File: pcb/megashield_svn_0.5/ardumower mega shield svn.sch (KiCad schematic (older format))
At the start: 88 parts, among them K1 Tilt sens, K2 Button, K3 RELAY_2RT, P1 Sonar C, P10 GPS, P11 Bumper, P12 PerimeterRight, P13 RC Remote, P14 User switch, P15 Dual2-M1Out, P16 Dual2-pwr, P17 Dual1-pwr, P18 Mow Motor, P19 DS1307, P2 Sonar R, P20 Wlan, P21 DropRight, P3 Sonar L, P4 Rain, P5 IMU Kompas, P6 Lawn sens, P7 Status LEDs, P8 ODO Right, P9 ODO Left, U1 DC-DC, U2 HC05_Bluetooth, U3 INA169 Adafruit

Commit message: Pufferkondensator 3,3V + 5,5V , Spannungsleiste 3,3V +5V +GND, Pins unbenutzte Kontakte hinzugefügt Regensensor hat jetzt auch 5V + kleine Änderungen
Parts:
- removed P4: Rain, Pin_Headers:Pin_Header_Straight_1x02, symbol CONN_2
- added C? (x2): ??, Capacitors_ThroughHole:Capacitor3MMDiscRM2.5, symbol CP1
- added JP?: 5V, Connect:PINHEAD1-2, symbol JUMPER
- added JP?: 3,3V, Connect:PINHEAD1-2, symbol JUMPER
- added P4: Rain, Pin_Headers:Pin_Header_Straight_1x03, symbol CONN_3
- added P? (x5): CONN_01X01, symbol CONN_01X01
- added P?: Stromleiste 5V, symbol CONN_01X08
- added P?: Stromleiste GND, symbol CONN_01X08
- added P?: Stromleiste 3,3V, symbol CONN_01X08
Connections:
- net +3.3V: now also C?.1, JP?.1, P?.1 (P1), P?.2 (P2), P?.3 (P3), P?.4 (P4), P?.5 (P5), P?.6 (P6), P?.7 (P7), P?.8 (P8)
- net +5V: now also C?.1, JP?.1, P4.1 (P1), P?.1 (P1), P?.2 (P2), P?.3 (P3), P?.4 (P4), P?.5 (P5), P?.6 (P6), P?.7 (P7), P?.8 (P8); no longer U2.6 (VCC)
- net GND: now also C?.2, C?.2, P4.3 (P3), P?.1 (P1), P?.2 (P2), P?.3 (P3), P?.4 (P4), P?.5 (P5), P?.6 (P6), P?.7 (P7), P?.8 (P8)
- net pinRain: now also P4.2 (PM)
- net at SHIELD1.0 (RX0): now also P?.1 (P1)
- net at SHIELD1.1 (TX0): now also P?.1 (P1)
- net at SHIELD1.4: now also P?.1 (P1)
- net at SHIELD1.8: now also P?.1 (P1)
- net at SHIELD1.9: now also P?.1 (P1)
- new net: JP?.2, JP?.2, U2.6 (VCC)
- no-connect marks 41 -> 36
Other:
- note added: "Abgriff 5V, 3V, GND"
- note added: "Pufferkondensator 3,3v und 5V\ndamit könten eigentlich die\neinzelnen Kondensatoren entfallen.\nz.B bei den INA"
- note removed: "VCC muss das nicht auch 3.3V sein\n?????????????????????????????"
- moved on the sheet: R1, R2, R5, R?

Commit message: Änderungen am Schaltplan, Footprint und PCB Achtung Relais fehlerhaft ! Anordung der Bauteile muss noch Feintunig erfolgen
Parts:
- removed C? (x2): ??, Capacitors_ThroughHole:Capacitor3MMDiscRM2.5, symbol CP1
- P22, P23, P24, P25, P26, P27, P28, P29: renamed from P?; footprint (none) -> Pin_Headers:Pin_Header_Straight_1x01
- P32, P33, P34: renamed from P?; footprint (none) -> Pin_Headers:Pin_Header_Straight_1x08
- P4: footprint Pin_Headers:Pin_Header_Straight_1x03 -> Pin_Headers:Pin_Header_Straight_1x02
- P7: footprint (none) -> Pin_Headers:Pin_Header_Straight_1x04
- Q1: renamed from Q?; footprint TO92-EBC -> Discret:TO92-EBC
- R18: renamed from R?; footprint (none) -> Resistors_ThroughHole:Resistor_Horizontal_RM15mm
- RR2: footprint Pin_Headers:Pin_Header_Straight_1x04 -> Pin_Headers:Pin_Header_Straight_1x09
- gave numbers to parts that had none: 26
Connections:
- net GND: now also K1.2 (PM), P1.2 (P2), P2.2 (P2), P3.2 (P2), P30.2 (PM), P4.2 (PM), P5.2 (P2), P8.2 (P2), P9.2 (P2); no longer K1.3 (P3), P1.4 (P4), P2.4 (P4), P3.4 (P4), P30.3 (P3), P4.3 (P3), P5.4 (P4), P8.4 (P4), P9.4 (P4)
- net SCL1: now also P5.4 (P4); no longer P5.3 (P3)
- net SDA1: now also P5.3 (P3); no longer P5.2 (P2)
- net pinBatteryVoltage: now also RP1.11 (R6); no longer RP1.3 (P3)
- net pinChargeCurrent: now also RP2.9 (R8); no longer RP2.1 (P1)
- net pinChargeVoltage: now also RP2.10 (R7); no longer RP2.2 (P2)
- net pinChargingBilanz: now also RP2.11 (R6); no longer RP2.3 (P3)
- net pinMotorLeftSense: now also RP1.10 (R7); no longer RP1.2 (P2)
- net pinMotorMowSense: now also RP1.12 (R5); no longer RP1.4 (P4)
- net pinMotorRightSense: now also RP1.9 (R8); no longer RP1.1 (P1)
- net pinOdometryLeft: now also P9.3 (P3), RP2.13 (R4); no longer P9.2 (P2), RP2.5 (P5)
- net pinOdometryLeft2: now also P9.4 (P4), RP2.14 (R3); no longer P9.3 (P3), RP2.6 (P6)
- net pinOdometryRight: now also P8.3 (P3), RP2.15 (R2); no longer P8.2 (P2), RP2.8 (P8)
- net pinOdometryRight2: now also P8.4 (P4), RP2.16 (R1); no longer P8.3 (P3), RP2.7 (P7)
- net pinPerimeterLeft: now also RP1.14 (R3); no longer RP1.6 (P6)
- net pinPerimeterRight: now also P30.3 (P3), RP1.13 (R4); no longer P30.2 (PM), RP1.5 (P5)
- net pinRain: now also P4.3 (P3); no longer P4.2 (PM)
- net pinSonarCenterEcho: now also P1.4 (P4); no longer P1.3 (P3)
- net pinSonarCenterTrigger: now also P1.3 (P3); no longer P1.2 (P2)
- net pinSonarLeftEcho: now also P3.4 (P4); no longer P3.3 (P3)
- net pinSonarLeftTrigger: now also P3.3 (P3); no longer P3.2 (P2)
- net pinSonarRightEcho: now also P2.4 (P4); no longer P2.3 (P3)
- net pinSonarRightTrigger: now also P2.3 (P3); no longer P2.2 (P2)
- net pinTilt: now also K1.3 (P3); no longer K1.2 (PM)
- net at RR1.2, SHIELD1.AD0: now also RP1.8 (P8); no longer RP1.16 (R1)
- net at RR1.3, SHIELD1.AD1: now also RP1.7 (P7); no longer RP1.15 (R2)
- net at RR2.4, SHIELD1.AD10: now also RP2.6 (P6); no longer RP2.14 (R3)
- net at RR2.5, SHIELD1.AD11: now also RP2.5 (P5); no longer RP2.13 (R4)
- net at RR2.6, SHIELD1.AD12: now also RP2.4 (P4); no longer RP2.12 (R5)
- net at RR2.7, SHIELD1.AD13: now also RP2.3 (P3); no longer RP2.11 (R6)
- net at RR2.8, SHIELD1.AD14: now also RP2.2 (P2); no longer RP2.10 (R7)
- net at RR2.9, SHIELD1.AD15: now also RP2.1 (P1); no longer RP2.9 (R8)
- net at RR1.4, SHIELD1.AD2: now also RP1.6 (P6); no longer RP1.14 (R3)
- net at RR1.5, SHIELD1.AD3: now also RP1.5 (P5); no longer RP1.13 (R4)
- net at RR1.6, SHIELD1.AD4: now also RP1.4 (P4); no longer RP1.12 (R5)
- net at RR1.7, SHIELD1.AD5: now also RP1.3 (P3); no longer RP1.11 (R6)
- net at RR1.8, SHIELD1.AD6: now also RP1.2 (P2); no longer RP1.10 (R7)
- net at RR1.9, SHIELD1.AD7: now also RP1.1 (P1); no longer RP1.9 (R8)
- net at RR2.2, SHIELD1.AD8: now also RP2.8 (P8); no longer RP2.16 (R1)
- net at RR2.3, SHIELD1.AD9: now also RP2.7 (P7); no longer RP2.15 (R2)
- net at P22.1 (P1): now also RP1.15 (R2); no longer RP1.7 (P7)
- net at P23.1 (P1): now also RP1.16 (R1); no longer RP1.8 (P8)
- net at P24.1 (P1): now also RP2.12 (R5); no longer RP2.4 (P4)
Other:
- note removed: "Pufferkondensator 3,3v und 5V\ndamit könten eigentlich die\neinzelnen Kondensatoren entfallen.\nz.B bei den INA"

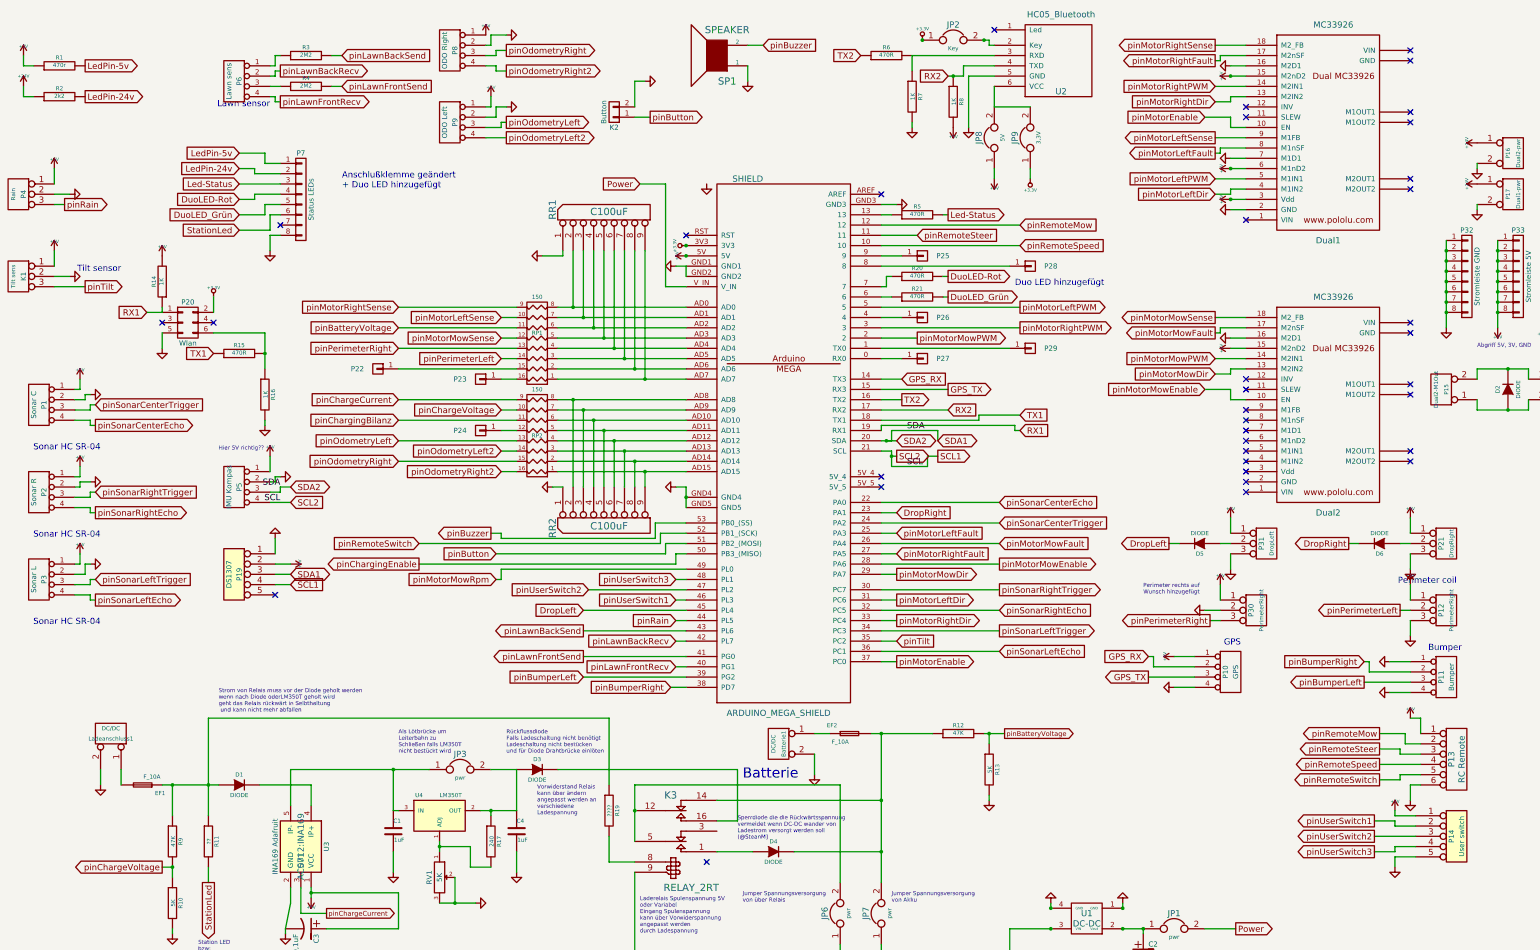
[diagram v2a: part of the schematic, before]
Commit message: Angefangen Platinenlayout zu erstellen Fehler vorhanden die Netzlinien der 2 INA169 enden an der Schraubenbefestigung und nicht an den Klemmen Der Footprint von P7 Status LED ist nur 4 Fach muss 8 fach sein Der Footprint von den Jumpern J2, J8, J9 ist falsch - zu groß der muss kleiner sein wie die anderen Jumper Kann selber die Footprints nicht zuordnen. Ich bekomme immer eine Fehlermeldung mit einen "Bibliothek Pfad" der wahrscheinlich auf ein Ordner von Stefan seine Festplatte verweist.
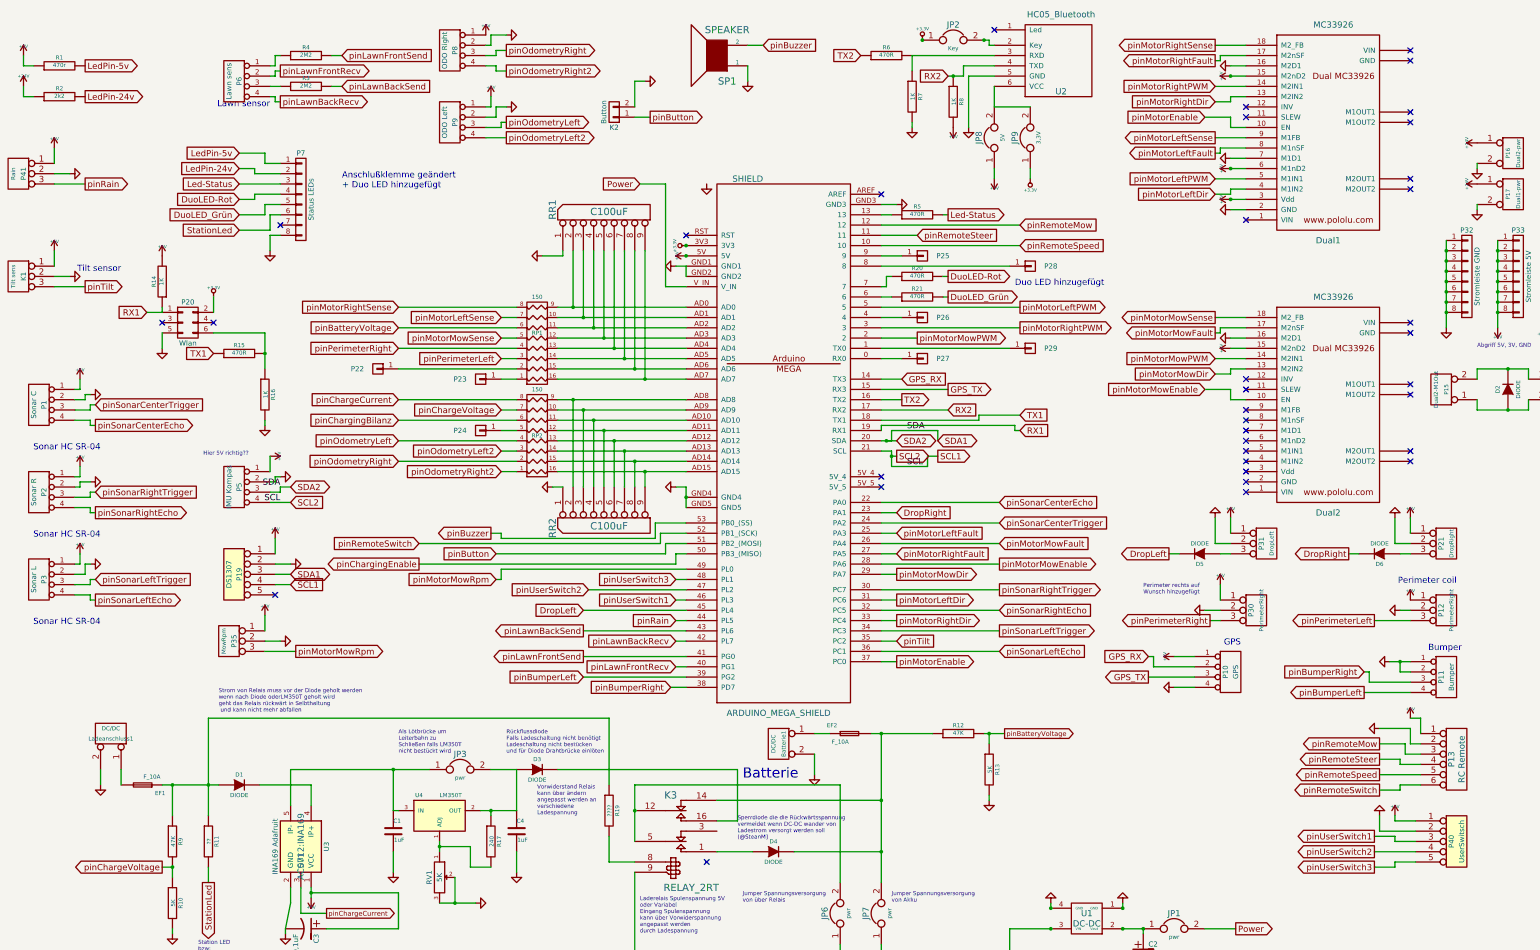
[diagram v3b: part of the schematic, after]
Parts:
- removed P14: User switch, Pin_Headers:Pin_Header_Straight_1x06, symbol CONN_5
- removed P4: Rain, Pin_Headers:Pin_Header_Straight_1x02, symbol CONN_3
- added P35: MowRpm, Pin_Headers:Pin_Header_Straight_1x03, symbol CONN_3
- added P40: UserSwitsch, Pin_Headers:Pin_Header_Straight_1x05, symbol CONN_5
- added P41: Rain, Pin_Headers:Pin_Header_Straight_1x03, symbol CONN_3
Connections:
- net +5V: now also P19.1, P35.1 (P1), P40.1, P41.1 (P1); no longer P19.2
- net GND: now also P11.2 (P2), P12.2 (PM), P13.2, P19.2, P21.2 (PM), P31.2 (PM), P35.2 (PM), P40.2, P41.2 (PM); no longer P11.4 (P4), P12.3 (P3), P13.6, P19.1, P21.3 (P3), P31.3 (P3)
- net pinBatteryVoltage: now also RP1.6 (P6); no longer RP1.11 (R6)
- net pinBumperLeft: now also P11.4 (P4); no longer P11.3 (P3)
- net pinBumperRight: now also P11.3 (P3); no longer P11.2 (P2)
- net pinChargeCurrent: now also RP2.8 (P8); no longer RP2.9 (R8)
- net pinChargeVoltage: now also RP2.7 (P7); no longer RP2.10 (R7)
- net pinChargingBilanz: now also RP2.6 (P6); no longer RP2.11 (R6)
- net pinLawnBackRecv: now also P6.4 (P4); no longer P6.2 (P2)
- net pinLawnFrontRecv: now also P6.2 (P2); no longer P6.4 (P4)
- net pinMotorLeftSense: now also RP1.7 (P7); no longer RP1.10 (R7)
- net pinMotorMowRpm: now also P35.3 (P3)
- net pinMotorMowSense: now also RP1.5 (P5); no longer RP1.12 (R5)
- net pinMotorRightSense: now also RP1.8 (P8); no longer RP1.9 (R8)
- net pinOdometryLeft: now also RP2.4 (P4); no longer RP2.13 (R4)
- net pinOdometryLeft2: now also RP2.3 (P3); no longer RP2.14 (R3)
- net pinOdometryRight: now also RP2.2 (P2); no longer RP2.15 (R2)
- net pinOdometryRight2: now also RP2.1 (P1); no longer RP2.16 (R1)
- net pinPerimeterLeft: now also P12.3 (P3), RP1.3 (P3); no longer P12.2 (PM), RP1.14 (R3)
- net pinPerimeterRight: now also RP1.4 (P4); no longer RP1.13 (R4)
- net pinRain: now also P41.3 (P3)
- net pinRemoteMow: now also P13.3; no longer P13.2
- net pinRemoteSpeed: now also P13.5; no longer P13.4
- net pinRemoteSteer: now also P13.4; no longer P13.3
- net pinRemoteSwitch: now also P13.6; no longer P13.5
- net pinUserSwitch1: now also P40.3
- net pinUserSwitch2: now also P40.4
- net pinUserSwitch3: now also P40.5
- net at RR1.2, SHIELD1.AD0: now also RP1.9 (R8); no longer RP1.8 (P8)
- net at RR1.3, SHIELD1.AD1: now also RP1.10 (R7); no longer RP1.7 (P7)
- net at RR2.4, SHIELD1.AD10: now also RP2.11 (R6); no longer RP2.6 (P6)
- net at RR2.5, SHIELD1.AD11: now also RP2.12 (R5); no longer RP2.5 (P5)
- net at RR2.6, SHIELD1.AD12: now also RP2.13 (R4); no longer RP2.4 (P4)
- net at RR2.7, SHIELD1.AD13: now also RP2.14 (R3); no longer RP2.3 (P3)
- net at RR2.8, SHIELD1.AD14: now also RP2.15 (R2); no longer RP2.2 (P2)
- net at RR2.9, SHIELD1.AD15: now also RP2.16 (R1); no longer RP2.1 (P1)
- net at RR1.4, SHIELD1.AD2: now also RP1.11 (R6); no longer RP1.6 (P6)
- net at RR1.5, SHIELD1.AD3: now also RP1.12 (R5); no longer RP1.5 (P5)
- net at RR1.6, SHIELD1.AD4: now also RP1.13 (R4); no longer RP1.4 (P4)
- net at RR1.7, SHIELD1.AD5: now also RP1.14 (R3); no longer RP1.3 (P3)
- net at RR1.8, SHIELD1.AD6: now also RP1.15 (R2); no longer RP1.2 (P2)
- net at RR1.9, SHIELD1.AD7: now also RP1.16 (R1); no longer RP1.1 (P1)
- net at RR2.2, SHIELD1.AD8: now also RP2.9 (R8); no longer RP2.8 (P8)
- net at RR2.3, SHIELD1.AD9: now also RP2.10 (R7); no longer RP2.7 (P7)
- net at P6.1 (P1): now also R4.1; no longer R3.1
- net at P6.3 (P3): now also R3.1; no longer R4.1
- net at P22.1 (P1): now also RP1.2 (P2); no longer RP1.15 (R2)
- net at P23.1 (P1): now also RP1.1 (P1); no longer RP1.16 (R1)
- net at D6.1 (A): now also P21.3 (P3); no longer P21.2 (PM)
- net at D5.1 (A): now also P31.3 (P3); no longer P31.2 (PM)
- net at P24.1 (P1): now also RP2.5 (P5); no longer RP2.12 (R5)
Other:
- moved on the sheet: D5, D6, R3, R4

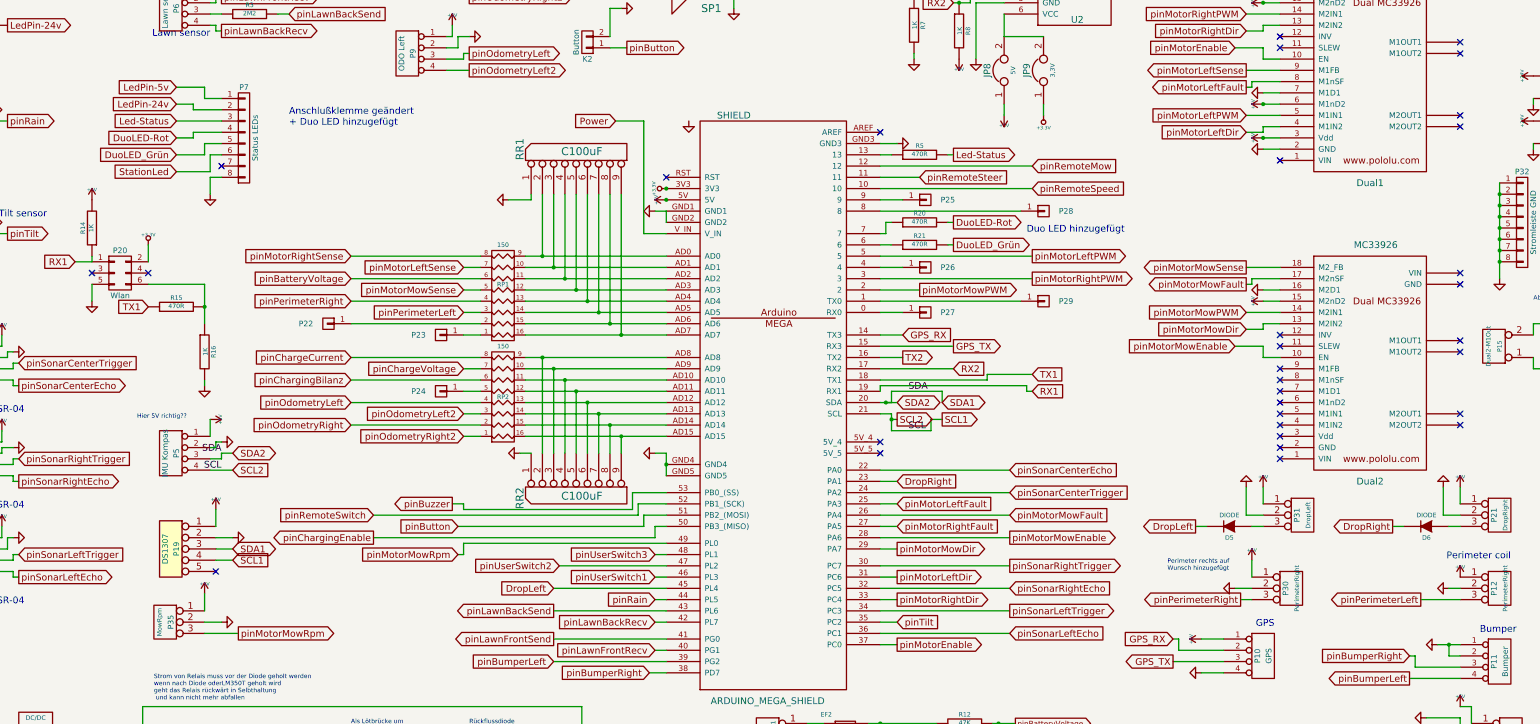
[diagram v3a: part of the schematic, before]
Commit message: Platinenlayout weiter gearbeitet Fehler vorhanden die Netzlinien der 2 INA169 enden an der Schraubenbefestigung und nicht an den Klemmen Der Fehler Footprint von P7 Status LED behoben Der Fehler Footprint von den Jumpern J2, J8, J9  behoben Fehlermeldung mit einen "Bibliothek Pfad" der wahrscheinlich auf ein Ordner von Stefan seine Festplatte verweist ist noch vohanden
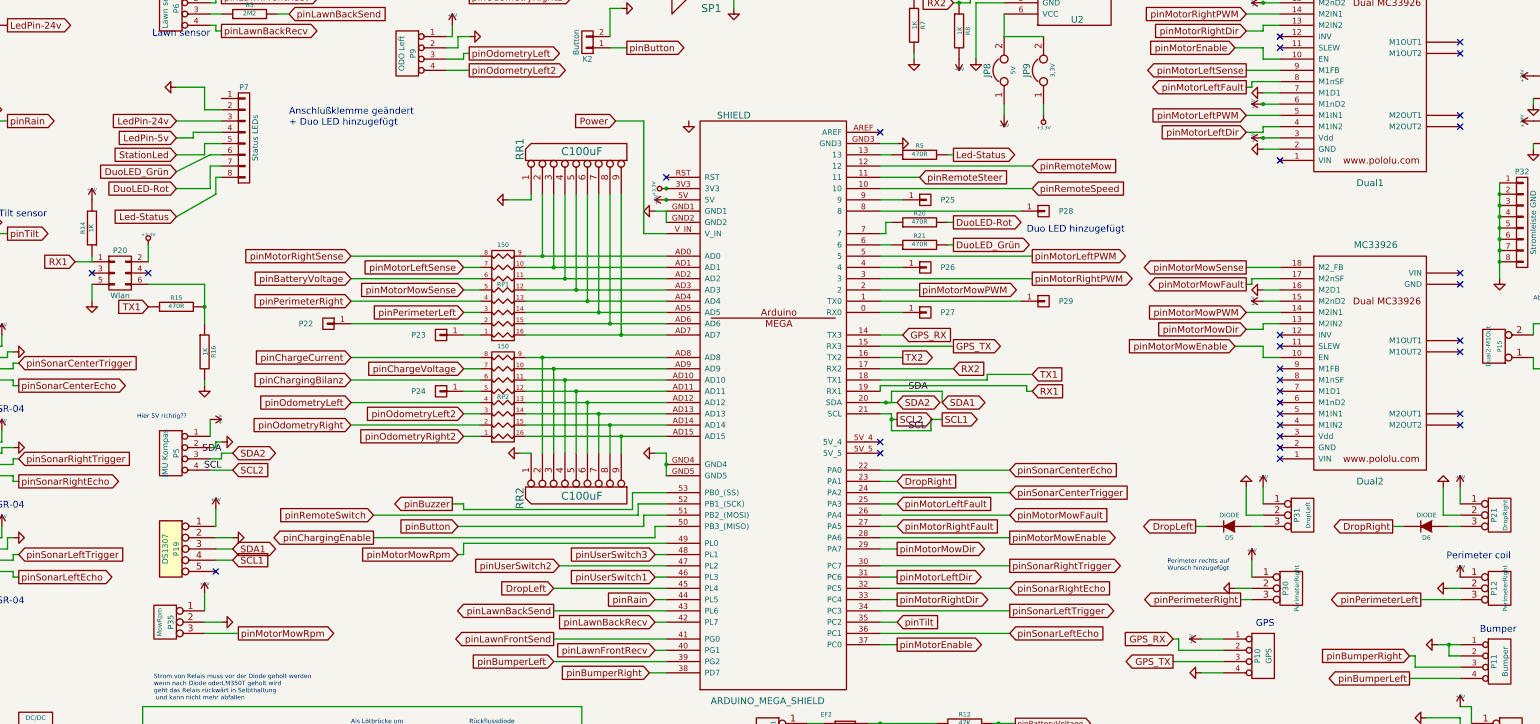
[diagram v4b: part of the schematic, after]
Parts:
- JP2, JP8, JP9: footprint Connect:PINHEAD1-2 -> Pin_Headers:Pin_Header_Straight_1x02
- P7: footprint Pin_Headers:Pin_Header_Straight_1x04 -> Pin_Headers:Pin_Header_Straight_1x08
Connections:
- net DuoLED-Rot: now also P7.7 (P7); no longer P7.4 (P4)
- net DuoLED_Grün: now also P7.6 (P6); no longer P7.5 (P5)
- net GND: now also P7.2 (P2); no longer P7.8 (P8)
- net Led-Status: now also P7.8 (P8); no longer P7.3 (P3)
- net LedPin-24v: now also P7.3 (P3); no longer P7.2 (P2)
- net LedPin-5v: now also P7.4 (P4); no longer P7.1 (P1)
- net StationLed: now also P7.5 (P5); no longer P7.6 (P6)
- no-connect marks 36 -> 35

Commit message: Footprints berichtigt
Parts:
- K3: footprint Relays_ThroughHole:Relais_DPDT_Schrack-RT2_RM5mm -> ACS712:Relais_DPDT_Schrack-RT2_RM5mm
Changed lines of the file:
@@
 LIBS:power
 LIBS:ardumower mega shield svn-cache
-EELAYER 25 0
+EELAYER 24 0
 EELAYER END
 $Descr A3 16535 11693
@@
 F 0 "K3" H 7050 8900 70  0000 C CNN
 F 1 "RELAY_2RT" H 7250 8000 70  0000 C CNN
-F 2 "Relays_ThroughHole:Relais_DPDT_Schrack-RT2_RM5mm" H 7100 8500 60  0001 C CNN
+F 2 "ACS712:Relais_DPDT_Schrack-RT2_RM5mm" H 7100 8500 60  0001 C CNN
 F 3 "" H 7100 8500 60  0000 C CNN
 	1    7100 8500
